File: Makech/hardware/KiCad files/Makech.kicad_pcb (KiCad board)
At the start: 2 copper layers, 55 x 110.1 mm, 99 parts, among them IC1 ULN2803, J1 SWD programmer, J2 USB_B_Micro, J3 ESP32-Exp, SW1 RST, SW2 SW_DPDT_x2, U1 ATSAMD21G18A-AU, U2 CONN_01X04, U3 AP2114_3.3v, X1 Screw_Terminal_1x02

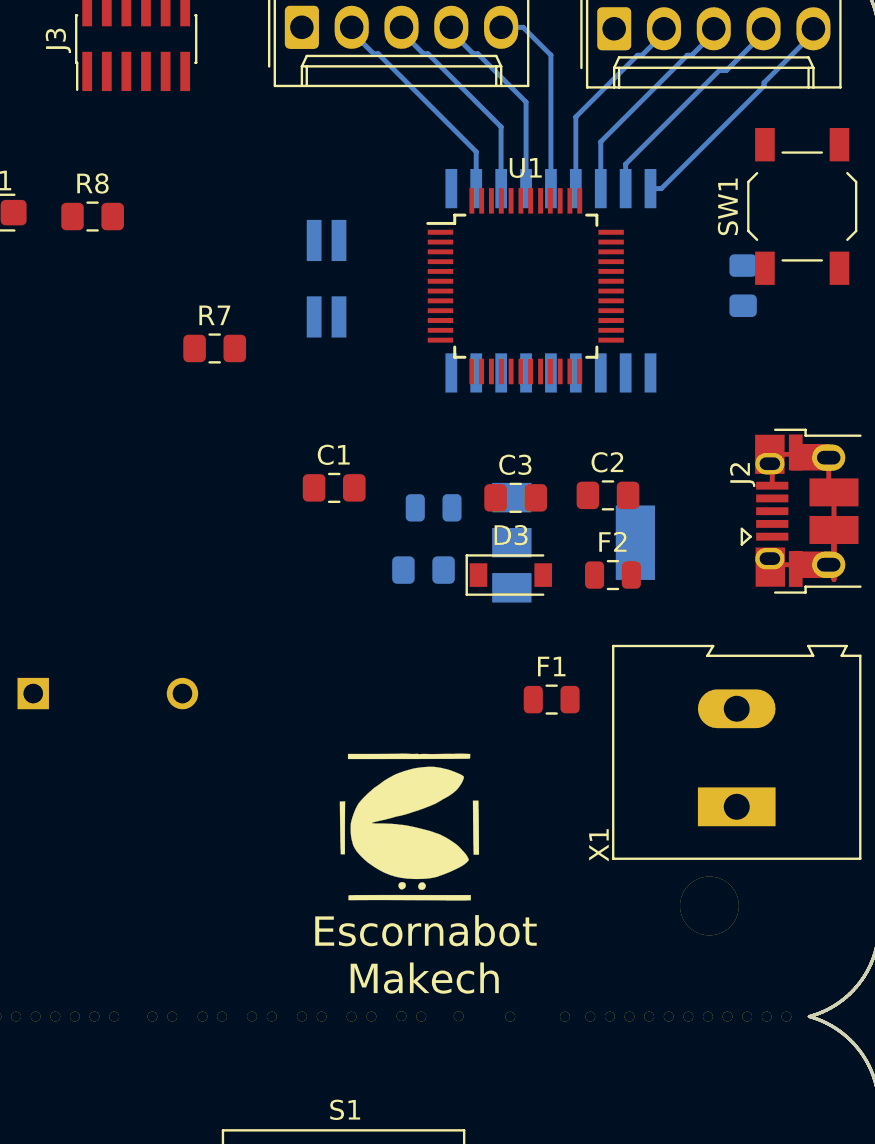
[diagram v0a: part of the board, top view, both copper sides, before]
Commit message: fix source motor pcb
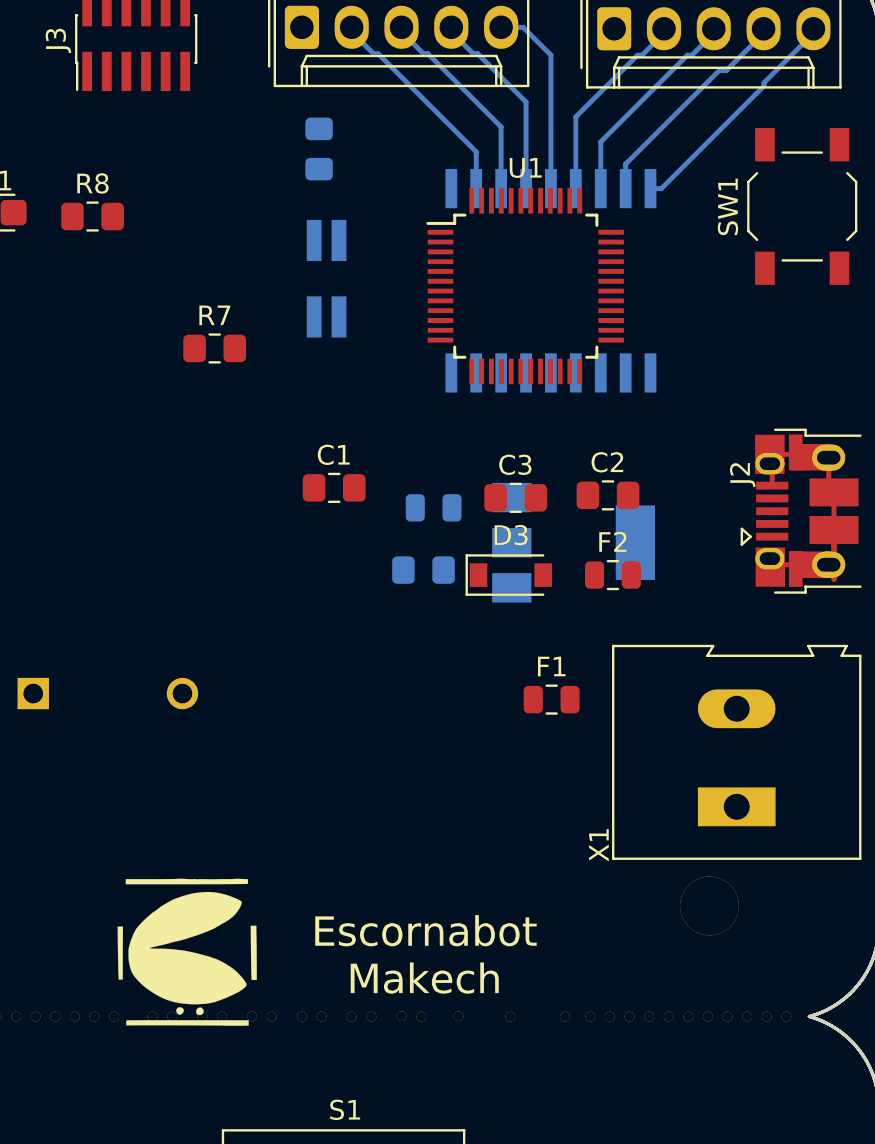
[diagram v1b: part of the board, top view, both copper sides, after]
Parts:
- moved C6 22.7 mm to (124.0, 45.5)
- moved G*** 13.0 mm to (117.2, 86.4)
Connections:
- XH1 pad 1: /RAW -> +6V
- XH2 pad 1: /RAW -> +6V
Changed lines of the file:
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@@
     (zones 0)
     (modules 99)
-    (nets 70)
+    (nets 69)
   )
   (page A4)
@@
   (net 66 "Net-(U1-Pad47)")
   (net 67 "Net-(U1-Pad48)")
-  (net 68 /RAW)
-  (net 69 "Net-(C4-Pad2)")
+  (net 68 "Net-(C4-Pad2)")
   (net_class Default "This is the default net class."
     (clearance 0.2)
@@
     (add_net /MR3)
     (add_net /MR4)
-    (add_net /RAW)
     (add_net /RX)
     (add_net /SCL)
@@
       (net 1 GND))
     (pad 2 smd roundrect (at 1.025 0) (size 1.15 1.4) (layers B.Cu B.Paste B.Mask) (roundrect_rratio 0.217391)
-      (net 69 "Net-(C4-Pad2)"))
+      (net 68 "Net-(C4-Pad2)"))
     (model ${KISYS3DMOD}/Capacitor_SMD.3dshapes/C_0805_2012Metric.wrl
       (at (xyz 0 0 0))
@@
   )
   (module Capacitor_SMD:C_0805_2012Metric_Pad1.15x1.40mm_HandSolder (layer B.Cu)
-    (at 145.575 52.425 90)
+    (at 123.952 45.457 90)
     (descr "Capacitor SMD 0805 (2012 Metric), square (rectangular) end terminal, IPC_7351 nominal with elongated pad for handsoldering. (Body size source: https://docs.google.com/spreadsheets/d/1BsfQQcO9C6DZCsRaXUlFlo91Tg2WpOkGARC1WS5S8t0/edit?usp=sharing), generated with kicad-footprint-generator")
     (tags "capacitor handsolder")
@@
       (net 8 +6V))
     (pad 1 smd rect (at -1.65 0) (size 0.9 1.2) (layers F.Cu F.Paste F.Mask)
-      (net 69 "Net-(C4-Pad2)"))
+      (net 68 "Net-(C4-Pad2)"))
     (model ${KISYS3DMOD}/Diode_SMD.3dshapes/D_SOD-123.wrl
       (at (xyz 0 0 0))
@@
     (fp_line (start -2.25 -1) (end 1.65 -1) (layer F.SilkS) (width 0.12))
     (pad 1 smd rect (at -1.65 0) (size 0.9 1.2) (layers F.Cu F.Paste F.Mask)
-      (net 69 "Net-(C4-Pad2)"))
+      (net 68 "Net-(C4-Pad2)"))
     (pad 2 smd rect (at 1.65 0) (size 0.9 1.2) (layers F.Cu F.Paste F.Mask)
       (net 10 VCC))
@@
       (net 7 +3V3))
     (pad 3 smd rect (at -3.15 -2.3) (size 2 1.5) (layers B.Cu B.Paste B.Mask)
-      (net 69 "Net-(C4-Pad2)"))
+      (net 68 "Net-(C4-Pad2)"))
     (pad 1 smd rect (at -3.15 2.3) (size 2 1.5) (layers B.Cu B.Paste B.Mask)
       (net 1 GND))
@@
       (net 25 /ML4))
     (pad 1 thru_hole roundrect (at 0 0) (size 1.74 2.2) (drill 1.2) (layers *.Cu *.Mask) (roundrect_rratio 0.143678)
-      (net 68 /RAW))
+      (net 8 +6V))
     (model ${KISYS3DMOD}/Connector_Molex.3dshapes/Molex_KK-254_AE-6410-05A_1x05_P2.54mm_Vertical.wrl
       (at (xyz 0 0 0))
@@
     )
     (pad 1 thru_hole roundrect (at 0 0) (size 1.74 2.2) (drill 1.2) (layers *.Cu *.Mask) (roundrect_rratio 0.143678)
-      (net 68 /RAW))
+      (net 8 +6V))
     (pad 2 thru_hole oval (at 2.54 0) (size 1.74 2.2) (drill 1.2) (layers *.Cu *.Mask)
       (net 21 /MR4))
@@
   )
   (module Aesthetics:escornabot_8x8 (layer F.Cu)
-    (at 128.55 79.975)
+    (at 117.221 86.36)
     (fp_text reference G*** (at 0 0) (layer F.SilkS) hide
       (effects (font (size 1.524 1.524) (thickness 0.3)))

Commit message: FOOTPRINT
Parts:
- JP1: value CONN_01X02 -> Jumper
- moved LED2 2.26 mm to (113.0, 123.2), turned to 90 degrees
- moved LED3 2.06 mm to (123.2, 130.8), turned to 0 degrees
- moved LED4 2.05 mm to (137.2, 121.9), turned to 90 degrees
- moved LED1 1.08 mm to (124.5, 111.8), turned to 0 degrees
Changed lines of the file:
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@@
-(kicad_pcb (version 20171130) (host pcbnew "(5.0.1-3-g963ef8bb5)")
+(kicad_pcb (version 20171130) (host pcbnew "(5.0.2)-1")
   (general
     (thickness 1.6)
@@
       (effects (font (size 1 1) (thickness 0.15)))
     )
-    (fp_text value CONN_01X02 (at 1.905 2.54 90) (layer F.Fab)
+    (fp_text value Jumper (at 1.905 2.54 90) (layer F.Fab)
       (effects (font (size 1 1) (thickness 0.15)))
     )
@@
   )
   (module LEDs:LED_D3.0mm (layer F.Cu)
-    (at 125.3 112.44 90)
+    (at 124.46 111.76)
     (descr "LED, diameter 3.0mm, 2 pins")
     (tags "LED diameter 3.0mm 2 pins")
-    (fp_text reference LED1 (at 1.27 -2.96 90) (layer F.SilkS)
+    (fp_text reference LED1 (at 1.27 -2.96) (layer F.SilkS)
       (effects (font (size 1 1) (thickness 0.15)))
     )
-    (fp_text value L (at 1.27 2.96 90) (layer F.Fab)
+    (fp_text value L (at 1.27 2.96) (layer F.Fab)
       (effects (font (size 1 1) (thickness 0.15)))
     )
@@
     (fp_arc (start 1.27 0) (end -0.29 -1.235516) (angle 108.8) (layer F.SilkS) (width 0.12))
     (fp_arc (start 1.27 0) (end -0.23 -1.16619) (angle 284.3) (layer F.Fab) (width 0.1))
-    (pad 2 thru_hole circle (at 2.54 0 90) (size 1.8 1.8) (drill 0.9) (layers *.Cu *.Mask)
+    (pad 2 thru_hole circle (at 2.54 0) (size 1.8 1.8) (drill 0.9) (layers *.Cu *.Mask)
       (net 46 "Net-(LED1-Pad2)"))
-    (pad 1 thru_hole rect (at 0 0 90) (size 1.8 1.8) (drill 0.9) (layers *.Cu *.Mask)
+    (pad 1 thru_hole rect (at 0 0) (size 1.8 1.8) (drill 0.9) (layers *.Cu *.Mask)
       (net 1 GND))
     (model ${KISYS3DMOD}/LEDs.3dshapes/LED_D3.0mm.wrl
@@
   )
   (module LEDs:LED_D3.0mm (layer F.Cu)
-    (at 111.63 121.41)
+    (at 113.03 123.19 90)
     (descr "LED, diameter 3.0mm, 2 pins")
     (tags "LED diameter 3.0mm 2 pins")
-    (fp_text reference LED2 (at 1.27 -2.96) (layer F.SilkS)
+    (fp_text reference LED2 (at 1.27 -2.96 90) (layer F.SilkS)
       (effects (font (size 1 1) (thickness 0.15)))
     )
-    (fp_text value L (at 1.27 2.96) (layer F.Fab)
+    (fp_text value L (at 1.27 2.96 90) (layer F.Fab)
       (effects (font (size 1 1) (thickness 0.15)))
     )
@@
     (fp_line (start 3.7 2.25) (end 3.7 -2.25) (layer F.CrtYd) (width 0.05))
     (fp_line (start 3.7 -2.25) (end -1.15 -2.25) (layer F.CrtYd) (width 0.05))
-    (pad 1 thru_hole rect (at 0 0) (size 1.8 1.8) (drill 0.9) (layers *.Cu *.Mask)
+    (pad 1 thru_hole rect (at 0 0 90) (size 1.8 1.8) (drill 0.9) (layers *.Cu *.Mask)
       (net 1 GND))
-    (pad 2 thru_hole circle (at 2.54 0) (size 1.8 1.8) (drill 0.9) (layers *.Cu *.Mask)
+    (pad 2 thru_hole circle (at 2.54 0 90) (size 1.8 1.8) (drill 0.9) (layers *.Cu *.Mask)
       (net 47 "Net-(LED2-Pad2)"))
     (model ${KISYS3DMOD}/LEDs.3dshapes/LED_D3.0mm.wrl
@@
   )
   (module LEDs:LED_D3.0mm (layer F.Cu)
-    (at 125.12 131.52 90)
+    (at 123.19 130.81)
     (descr "LED, diameter 3.0mm, 2 pins")
     (tags "LED diameter 3.0mm 2 pins")
-    (fp_text reference LED3 (at 1.27 -2.96 90) (layer F.SilkS)
+    (fp_text reference LED3 (at 1.27 -2.96) (layer F.SilkS)
       (effects (font (size 1 1) (thickness 0.15)))
     )
-    (fp_text value L (at 1.27 2.96 90) (layer F.Fab)
+    (fp_text value L (at 1.27 2.96) (layer F.Fab)
       (effects (font (size 1 1) (thickness 0.15)))
     )
@@
     (fp_arc (start 1.27 0) (end -0.29 -1.235516) (angle 108.8) (layer F.SilkS) (width 0.12))
     (fp_arc (start 1.27 0) (end -0.23 -1.16619) (angle 284.3) (layer F.Fab) (width 0.1))
-    (pad 2 thru_hole circle (at 2.54 0 90) (size 1.8 1.8) (drill 0.9) (layers *.Cu *.Mask)
+    (pad 2 thru_hole circle (at 2.54 0) (size 1.8 1.8) (drill 0.9) (layers *.Cu *.Mask)
       (net 48 "Net-(LED3-Pad2)"))
-    (pad 1 thru_hole rect (at 0 0 90) (size 1.8 1.8) (drill 0.9) (layers *.Cu *.Mask)
+    (pad 1 thru_hole rect (at 0 0) (size 1.8 1.8) (drill 0.9) (layers *.Cu *.Mask)
       (net 1 GND))
     (model ${KISYS3DMOD}/LEDs.3dshapes/LED_D3.0mm.wrl
@@
   )
   (module LEDs:LED_D3.0mm (layer F.Cu)
-    (at 138.82 120.71 180)
+    (at 137.16 121.92 90)
     (descr "LED, diameter 3.0mm, 2 pins")
     (tags "LED diameter 3.0mm 2 pins")
-    (fp_text reference LED4 (at 1.27 -2.96 180) (layer F.SilkS)
+    (fp_text reference LED4 (at 1.27 -2.96 90) (layer F.SilkS)
       (effects (font (size 1 1) (thickness 0.15)))
     )
-    (fp_text value L (at 1.27 2.96 180) (layer F.Fab)
+    (fp_text value L (at 1.27 2.96 90) (layer F.Fab)
       (effects (font (size 1 1) (thickness 0.15)))
     )
@@
     (fp_line (start 3.7 2.25) (end 3.7 -2.25) (layer F.CrtYd) (width 0.05))
     (fp_line (start 3.7 -2.25) (end -1.15 -2.25) (layer F.CrtYd) (width 0.05))
-    (pad 1 thru_hole rect (at 0 0 180) (size 1.8 1.8) (drill 0.9) (layers *.Cu *.Mask)
+    (pad 1 thru_hole rect (at 0 0 90) (size 1.8 1.8) (drill 0.9) (layers *.Cu *.Mask)
       (net 1 GND))
-    (pad 2 thru_hole circle (at 2.54 0 180) (size 1.8 1.8) (drill 0.9) (layers *.Cu *.Mask)
+    (pad 2 thru_hole circle (at 2.54 0 90) (size 1.8 1.8) (drill 0.9) (layers *.Cu *.Mask)
       (net 49 "Net-(LED4-Pad2)"))
     (model ${KISYS3DMOD}/LEDs.3dshapes/LED_D3.0mm.wrl

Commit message: PCB
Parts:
- JP1: footprint Connector_Wire:SolderWirePad_1x02_P3.81mm_Drill0.8mm -> Jumper:SolderJumper-2_P1.3mm_Bridged_RoundedPad1.0x1.5mm
- moved R5 37.7 mm to (138.7, 102.9)
- moved R6 37.5 mm to (138.7, 100.3)
- moved SW1 35.8 mm to (113.0, 52.1), turned to 0 degrees
- moved D1 35.1 mm to (132.1, 73.7)
- moved J3 30.4 mm to (135.0, 62.5), turned to 0 degrees
- moved U1 24.1 mm to (113.0, 63.5)
- moved D2 23.2 mm to (125.7, 71.1)
- moved R8 19.0 mm to (128.0, 59.7)
- moved C2 15.5 mm to (123.2, 63.5)
- moved IC1 12.7 mm to (135.8, 64.9)
- moved C6 12.7 mm to (124.0, 58.2)
- moved J1 12.7 mm to (124.3, 64.8)
- moved R7 12.3 mm to (128.0, 63.5)
- moved D3 12.1 mm to (125.7, 76.2)
- moved R11 12.0 mm to (119.1, 128.3), turned to 180 degrees
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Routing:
- net GND: track 16.7 -> 0.00 mm

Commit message: fix pcb
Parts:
- removed ? (x6): hole, ComponentesVarios:hole_3mm
- removed ? (x39): , ComponentesVarios:hole_05mm
- removed svg2mod: G***, borde:svg2mod
- removed svg2mod: G***, borde_S:svg2mod
- J2: footprint Connector_USB:USB_Micro-B_Amphenol_10103594-0001LF_Horizontal -> Connector_USB:USB_Micro-B_Wuerth_629105150521
- Z1: moved to F.Cu
- moved SW1 42.0 mm to (110.5, 94.0)
- moved SW2 35.8 mm to (100.3, 88.9)
- moved XH1 23.7 mm to (118.6, 62.9)
- moved XH2 23.1 mm to (103.4, 62.8)
- moved U1 22.7 mm to (133.3, 73.7)
- moved JP1 13.5 mm to (110.5, 87.6), turned to 180 degrees
- moved J2 11.8 mm to (147.3, 74.9)
- moved X1 11.2 mm to (144.8, 90.2)
- moved F2 11.2 mm to (141.0, 78.7)
- moved C1 10.9 mm to (123.7, 70.5)
- moved C2 10.9 mm to (123.7, 74.3)
- moved C3 10.9 mm to (123.7, 78.2)
- moved C4 10.9 mm to (130.3, 89.2)
- moved C6 10.9 mm to (124.5, 69.0)
- moved D3 10.9 mm to (126.2, 87.0)
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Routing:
- net /ML1: track 11.9 -> 0.00 mm
- net /ML2: track 11.3 -> 0.00 mm
- net /MR4: track 11.0 -> 0.00 mm
- net /ML3: track 10.7 -> 0.00 mm
- net /MR3: track 10.5 -> 0.00 mm
- net /ML4: track 10.1 -> 0.00 mm
- net /MR2: track 9.94 -> 0.00 mm
- net /MR1: track 9.93 -> 0.00 mm
- removed copper zone on B.Cu, net GND
- removed copper zone on F.Cu, net GND
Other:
- board size 55 x 110.1 mm -> 54.9 x 88.5 mm

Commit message: fix2 pcb
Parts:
- removed R7, R8: 10K, Resistor_SMD:R_0805_2012Metric_Pad1.15x1.40mm_HandSolder
- D1, D2, D3: moved to B.Cu
- moved C2 27.9 mm to (150.8, 67.7), turned to 270 degrees
- moved C3 25.5 mm to (147.0, 67.7), turned to 270 degrees
- moved SW1 21.1 mm to (129.8, 85.5)
- moved C1 11.0 mm to (133.7, 65.9)
- moved D1 8.53 mm to (124.5, 87.1)
- moved D2 8.52 mm to (118.4, 85.2)
- moved D3 8.28 mm to (118.4, 89.6)
- moved JP1 2.40 mm to (112.9, 87.7)
- moved J3 1.15 mm to (141.6, 62.9)
